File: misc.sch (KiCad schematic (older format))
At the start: 41 parts, among them CN8 POWER_INPUT, CN9 LED_CONNECTOR, SW1 SW_POWER, U10 NE555P, U12 74HCT02, U7 L7812, U9 74LS06

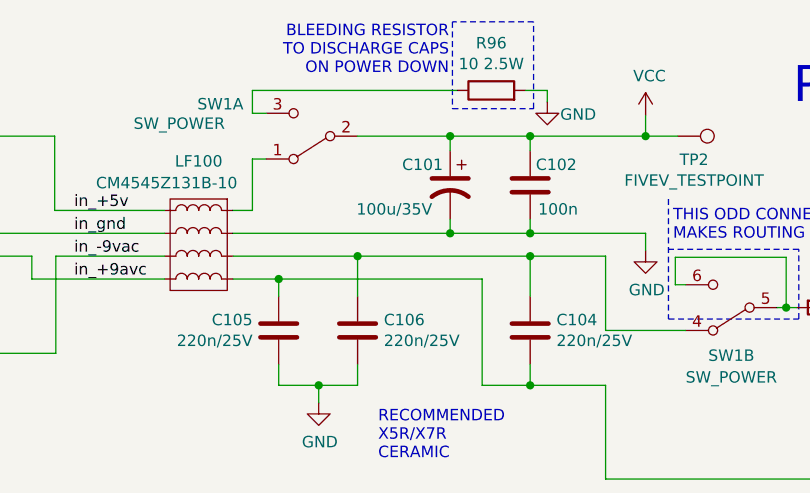
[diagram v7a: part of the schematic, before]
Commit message: Rationalize capacitor footprints & BOM
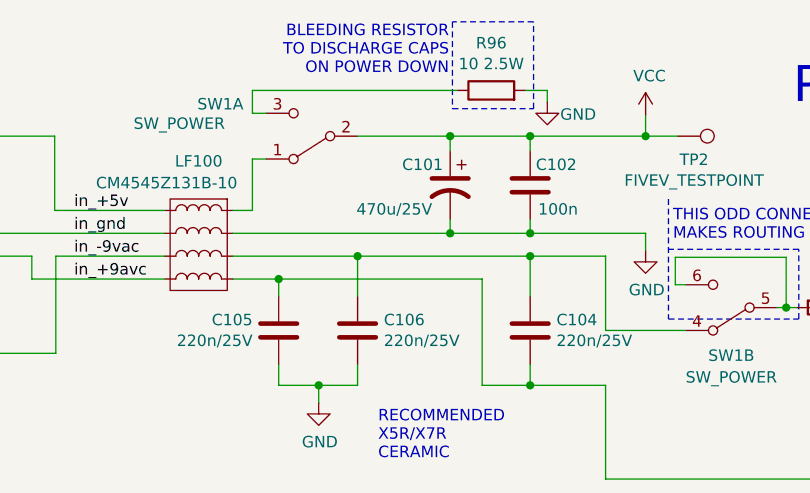
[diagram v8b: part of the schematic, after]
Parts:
- C101: value 100u/35V -> 470u/25V; footprint Capacitor_THT:CP_Radial_D8.0mm_P5.00mm -> Capacitor_THT:CP_Radial_D8.0mm_P3.50mm; MouserPN (none) -> 710-860010474013
- C16: footprint Capacitor_THT:CP_Radial_D6.3mm_P2.50mm -> Capacitor_THT:CP_Radial_D5.0mm_P2.00mm; MouserPN (none) -> 710-860010672009
- C17: footprint Capacitor_THT:CP_Radial_D6.3mm_P2.50mm -> Capacitor_THT:CP_Radial_D5.0mm_P2.00mm; MouserPN (none) -> 710-860010672005
- C95: footprint Capacitor_THT:CP_Radial_D10.0mm_P5.00mm -> Capacitor_THT:CP_Radial_D8.0mm_P3.50mm; MouserPN 710-860010575013 -> 710-860010474013
- LF100: MouserPN (none) -> 875-CM4545Z131B-10
- R21: MouserPN (none) -> 603-MFR-25FBF52-100K
- TP2, TP3, TP4: MouserPN (none) -> ---
- U12: MouserPN (none) -> 595-SN74HCT02N; Notes (none) -> Or 595-SN74HC02N, 595-SN74HCT02NE4
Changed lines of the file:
@@
 F 0 "C17" H 1791 4266 50  0000 R CNN
 F 1 "1u/16V" H 1791 4175 50  0000 R CNN
-F 2 "Capacitor_THT:CP_Radial_D6.3mm_P2.50mm" H 1905 4220 50  0001 C CNN
+F 2 "Capacitor_THT:CP_Radial_D5.0mm_P2.00mm" H 1905 4220 50  0001 C CNN
 F 3 "~" H 1905 4220 50  0001 C CNN
+F 4 "710-860010672005" H 1905 4220 50  0001 C CNN "MouserPN"
 	1    1905 4220
 	-1   0    0    -1
@@
 F 2 "Resistor_THT:R_Axial_DIN0207_L6.3mm_D2.5mm_P5.08mm_Vertical" V 1455 3460 50  0001 C CNN
 F 3 "~" H 1525 3460 50  0001 C CNN
+F 4 "603-MFR-25FBF52-100K" H 1525 3460 50  0001 C CNN "MouserPN"
 	1    1525 3460
 	-1   0    0    -1
@@
 F 0 "C16" H 4010 4516 50  0000 L CNN
 F 1 "10u/25V" H 4010 4425 50  0000 L CNN
-F 2 "Capacitor_THT:CP_Radial_D6.3mm_P2.50mm" H 3895 4470 50  0001 C CNN
+F 2 "Capacitor_THT:CP_Radial_D5.0mm_P2.00mm" H 3895 4470 50  0001 C CNN
 F 3 "~" H 3895 4470 50  0001 C CNN
+F 4 "710-860010672009" H 3895 4470 50  0001 C CNN "MouserPN"
 	1    3895 4470
 	-1   0    0    -1
@@
 AR Path="/5EACE220/62C8C494" Ref="C101"  Part="1"
 F 0 "C101" H 5405 1315 50  0000 R CNN
-F 1 "100u/35V" H 5605 1120 50  0000 R CNN
-F 2 "Capacitor_THT:CP_Radial_D8.0mm_P5.00mm" H 5195 1225 50  0001 C CNN
+F 1 "470u/25V" H 5605 1120 50  0000 R CNN
+F 2 "Capacitor_THT:CP_Radial_D8.0mm_P3.50mm" H 5195 1225 50  0001 C CNN
 F 3 "~" H 5195 1225 50  0001 C CNN
+F 4 "710-860010474013" H 5195 1225 50  0001 C CNN "MouserPN"
 	1    5195 1225
 	-1   0    0    -1
@@
 F 2 "LittleSixteen:CM4545Z131B-10" V 4095 1535 50  0001 C CNN
 F 3 "" V 4095 1535 50  0001 C CNN
+F 4 "875-CM4545Z131B-10" H 4095 1485 50  0001 C CNN "MouserPN"
 	1    4095 1485
 	-1   0    0    -1
@@
 F 0 "C95" H 10635 2341 50  0000 R CNN
 F 1 "470u/25V" H 10635 2250 50  0000 R CNN
-F 2 "Capacitor_THT:CP_Radial_D10.0mm_P5.00mm" H 10750 2295 50  0001 C CNN
+F 2 "Capacitor_THT:CP_Radial_D8.0mm_P3.50mm" H 10750 2295 50  0001 C CNN
 F 3 "~" H 10750 2295 50  0001 C CNN
-F 4 "710-860010575013" H 10750 2295 50  0001 C CNN "MouserPN"
+F 4 "710-860010474013" H 10750 2295 50  0001 C CNN "MouserPN"
 	1    10750 2295
 	-1   0    0    -1
@@
 F 2 "LittleSixteen:DIP-14_W7.62mm_Socket_LongPads" H 9805 6050 50  0001 C CNN
 F 3 "http://www.ti.com/lit/gpn/sn74ls02" H 9805 6050 50  0001 C CNN
+F 4 "595-SN74HCT02N" H 9805 6050 50  0001 C CNN "MouserPN"
+F 5 "Or 595-SN74HC02N, 595-SN74HCT02NE4" H 9805 6050 50  0001 C CNN "Notes"
 	4    9805 6050
 	1    0    0    -1
@@
 F 2 "TestPoint:TestPoint_Pad_D2.0mm" H 6935 6960 50  0001 C CNN
 F 3 "~" H 6935 6960 50  0001 C CNN
+F 4 "---" H 6735 6960 50  0001 C CNN "MouserPN"
 	1    6735 6960
 	-1   0    0    1
@@
 F 2 "TestPoint:TestPoint_Pad_D2.0mm" H 6390 1010 50  0001 C CNN
 F 3 "~" H 6390 1010 50  0001 C CNN
+F 4 "---" H 6190 1010 50  0001 C CNN "MouserPN"
 	1    6190 1010
 	0    1    1    0
@@
 F 2 "TestPoint:TestPoint_Pad_D2.0mm" H 9380 2145 50  0001 C CNN
 F 3 "~" H 9380 2145 50  0001 C CNN
+F 4 "---" H 9180 2145 50  0001 C CNN "MouserPN"
 	1    9180 2145
 	0    1    1    0
